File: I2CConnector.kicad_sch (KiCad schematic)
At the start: 10 parts, among them J5 I2C

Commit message: Change from TeensyIrrigation to PicoIrrigation and change the connectors. Will use breakout board for I2C MUX if necessary.
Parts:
- added Q5 (x2), Q6: Q_NMOS_GSD, Package_TO_SOT_SMD:SOT-23, symbol Device:Q_NMOS_GSD
- added R22 (x2), R23 (x2), R24, R25: 10kΩ, Resistor_SMD:R_0805_2012Metric, symbol Device:R
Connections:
- net +3.3V: now also Q5.1 (G), Q5.1 (G), Q6.1 (G), R23.2, R23.2, R24.2
- net +5V: no longer D1.2 (K), D2.2 (K)
- net INT: now also Q5.2 (S), R23.1; no longer D3.3 (A), J5.5 (Pin_5), R41.2
- net SCL: now also Q5.2 (S), R23.1; no longer D1.3 (A), J5.4 (Pin_4), R41.2
- net SDA: now also Q6.2 (S), R24.1; no longer D2.3 (A), J5.3 (Pin_3), R41.2
- net VBus renamed VI2C
- net VI2C: now also D1.2 (K), D2.2 (K), R22.2, R22.2, R25.2
- new net: D2.3 (A), J5.3 (Pin_3), Q6.3 (D), R25.1, R41.2
- new net: D1.3 (A), J5.4 (Pin_4), Q5.3 (D), R22.1, R41.2
- new net: D3.3 (A), J5.5 (Pin_5), Q5.3 (D), R22.1, R41.2

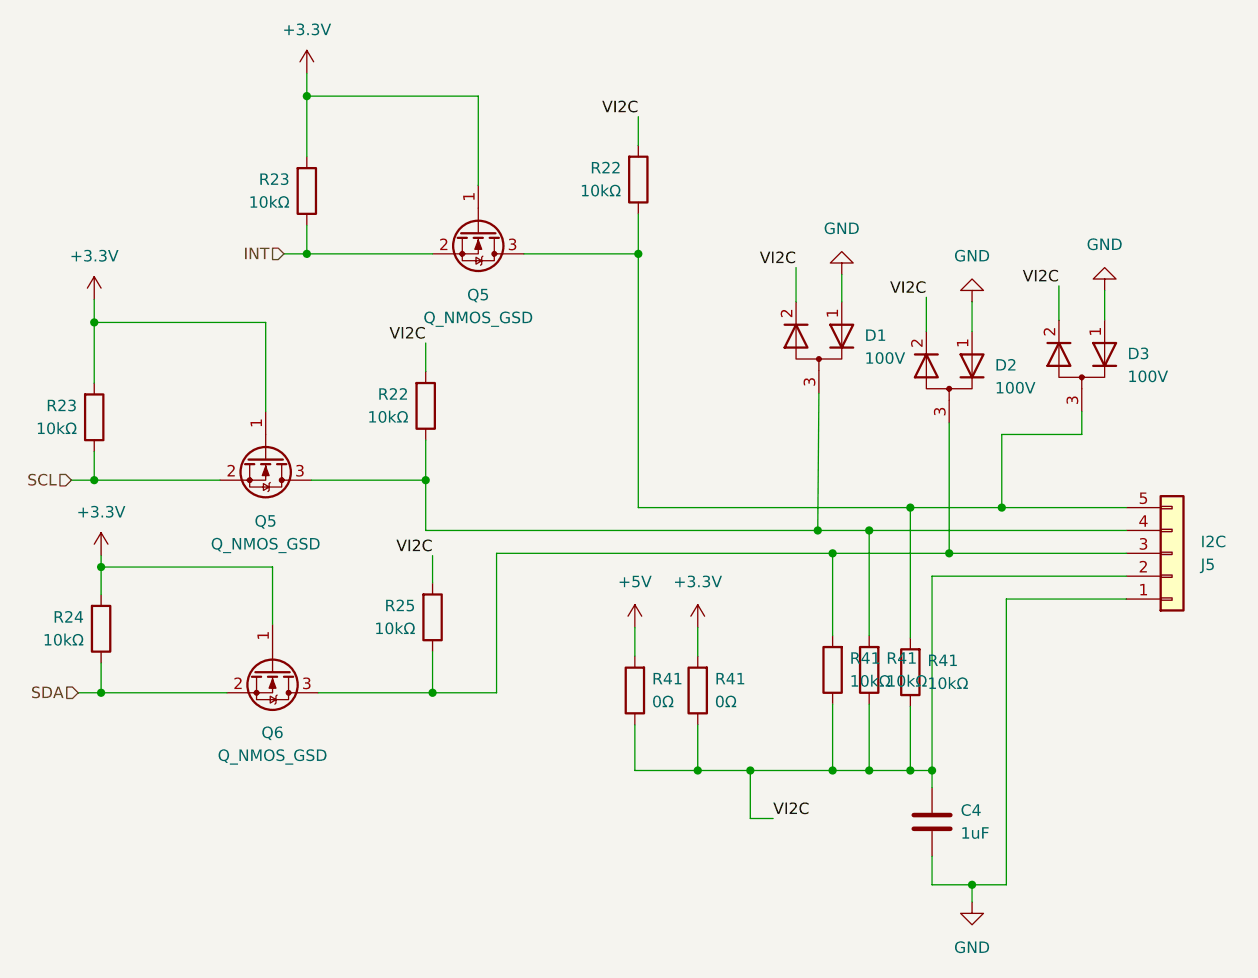
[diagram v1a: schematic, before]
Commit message: Finished schematic. Move to PCB.
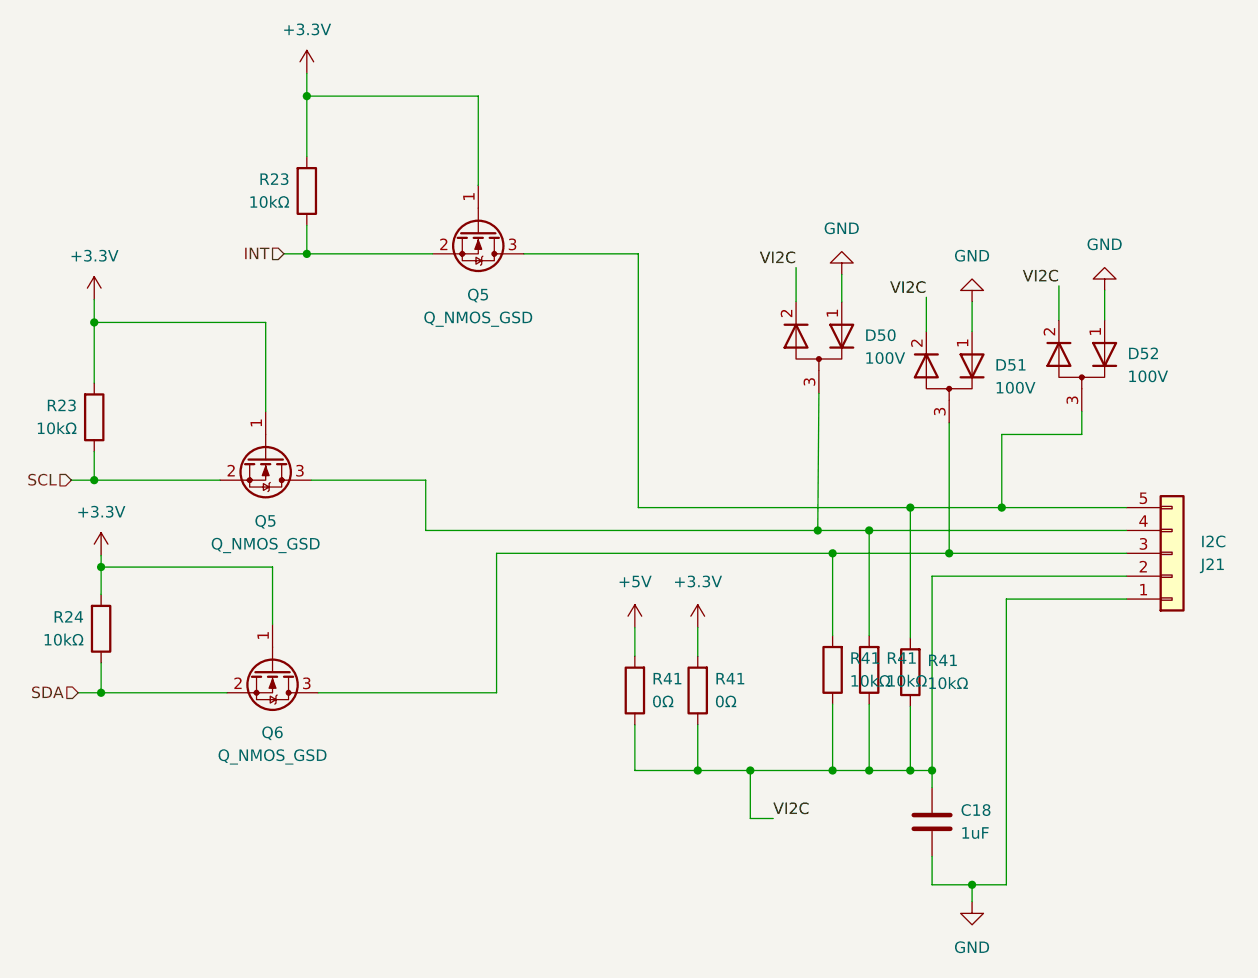
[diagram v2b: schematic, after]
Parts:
- removed R22 (x2), R25: 10kΩ, Resistor_SMD:R_0805_2012Metric, symbol Device:R
- renumbered C4 to C18, D1 to D50, D2 to D51, D3 to D52, J5 to J21
